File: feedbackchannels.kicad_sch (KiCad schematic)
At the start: 95 parts, among them J18 FB CH1, J19 FB CH2, J20 FB CH3, J21 FB CH4, J22 VDET CH1, J23 VDET CH2, Q1 SI7220 NMOS, U21 TLP2366, U22 TLP2366, U23 TLP2366, U24 TLP2366, U25 TLP2366, U26 TLP2366, U27 TLV7031, U28 TLV7031, U29 LTC4367, U30 TLP2366, U31 TLP2366, U32 74LVC1G126, U33 AP64350, U34 PCA9534

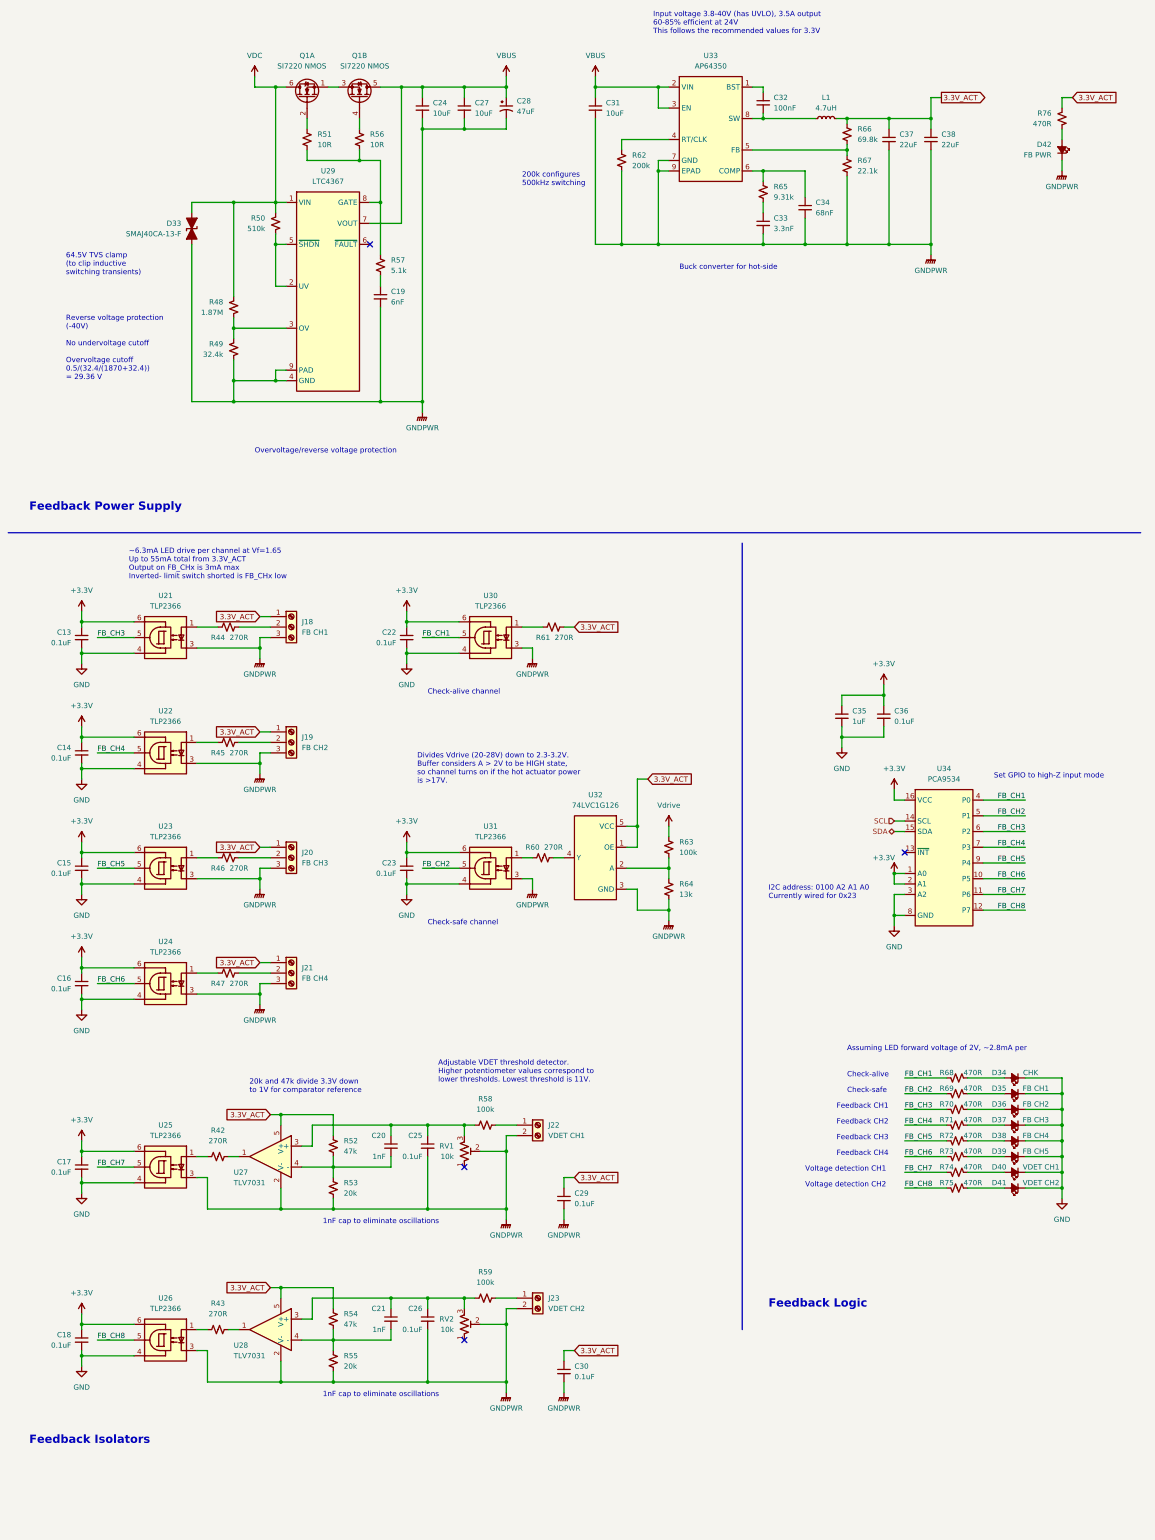
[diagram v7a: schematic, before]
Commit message: labeled chips with their function
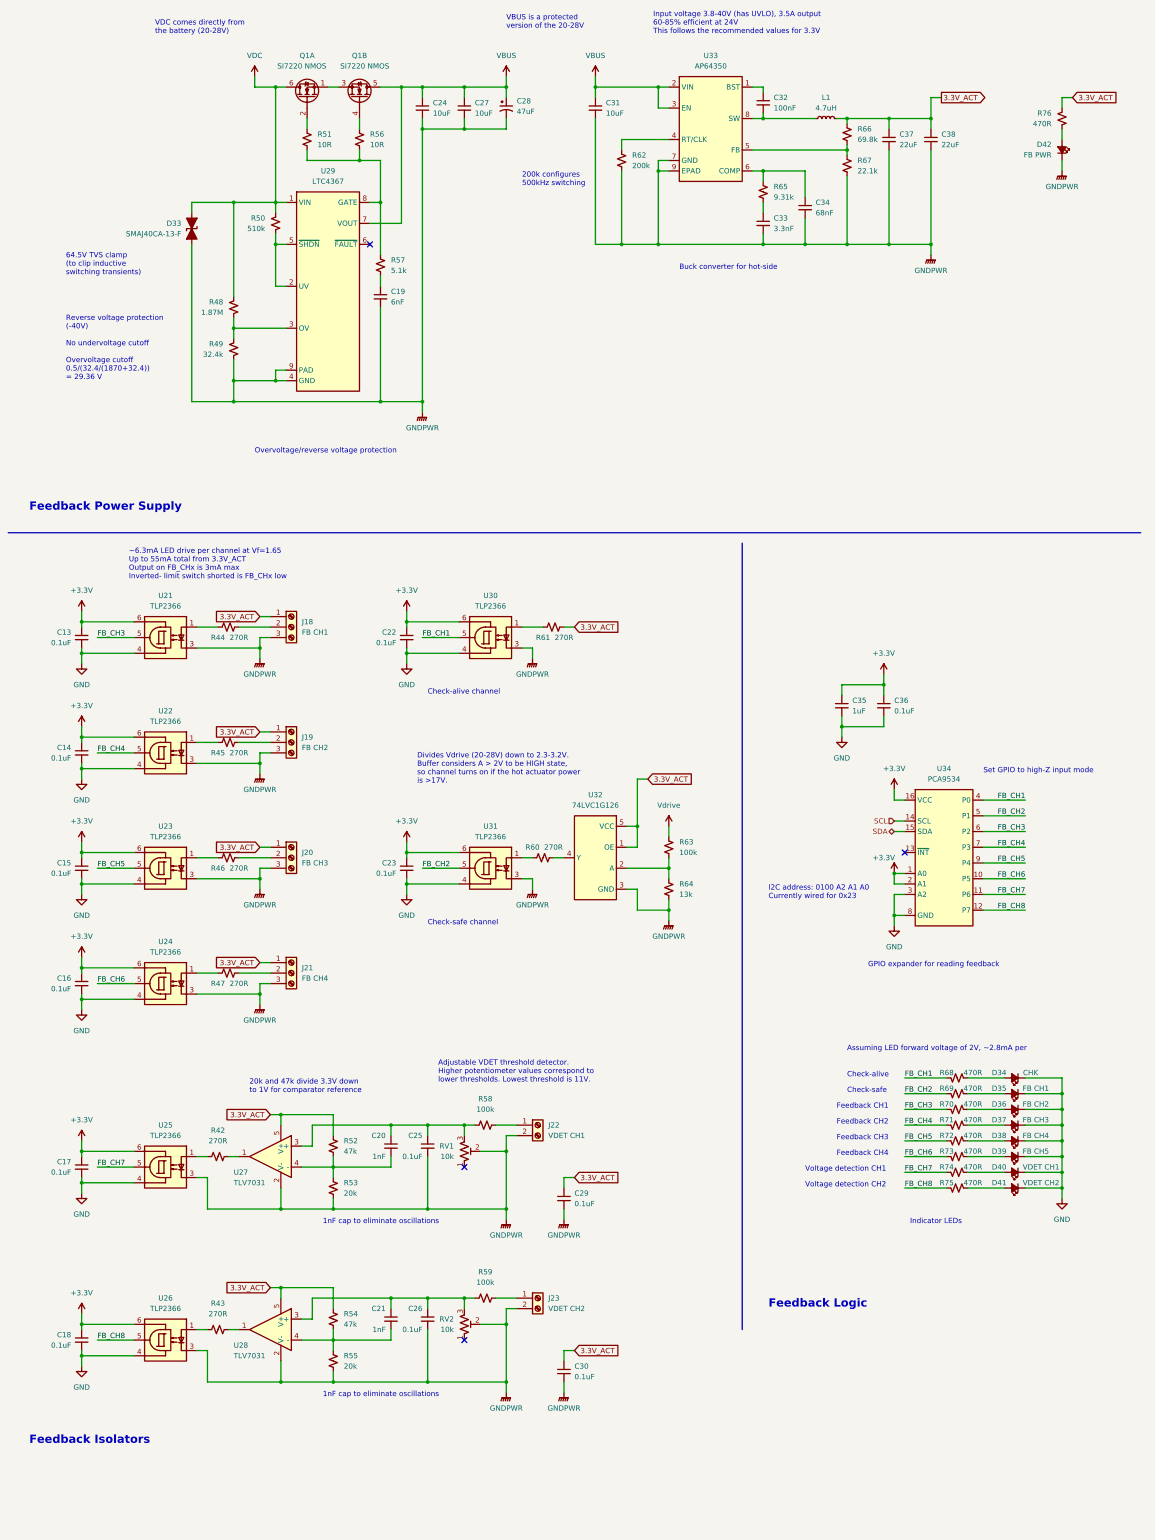
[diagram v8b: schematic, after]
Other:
- note added: "GPIO expander for reading feedback"
- note added: "Indicator LEDs"
- note added: "VBUS is a protected version of the 20-28V"
- note added: "VDC comes directly from the battery (20-28V)"
- moved on the sheet: C35, C36
